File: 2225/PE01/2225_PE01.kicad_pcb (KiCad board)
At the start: 2 copper layers, 95 parts, among them J4 Conn_01x01_Male

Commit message: Added rough board outline to PCB (dimensions are wrong).
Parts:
- moved CE3 45.1 mm to (216.4, 128.4)
- moved RE15 45.1 mm to (227.1, 132.3)
- moved CE12 45.1 mm to (249.7, 170.6)
- moved CE23 45.1 mm to (92.7, 143.0)
- moved CE24 45.1 mm to (92.7, 150.9)
- moved RE43 45.1 mm to (124.5, 133.8)
- moved 100k1 45.1 mm to (300.8, 145.6)
- moved 100k2 45.1 mm to (210.9, 148.1)
- moved CE10 45.1 mm to (270.8, 166.6)
- moved CE13 45.1 mm to (109.7, 159.8)
- moved CE14 45.1 mm to (109.7, 148.4)
- moved CE15 45.1 mm to (142.2, 167.8)
- moved CE17 45.1 mm to (183.9, 150.9)
- moved CE19 45.1 mm to (160.3, 131.0)
- moved CE2 45.1 mm to (332.5, 114.4)
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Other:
- board outline added: 281.9 x 71.4 mm

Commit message: Set PCB component positions to match holes on donor board
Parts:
- CE10, CE9: footprint Capacitor_THT:C_Rect_L7.2mm_W3.5mm_P5.00mm_FKS2_FKP2_MKS2_MKP2 -> Capacitor_THT:C_Rect_L7.2mm_W3.5mm_P8.50mm
- CE19, CE20: footprint Capacitor_THT:CP_Radial_D5.0mm_P2.50mm -> Capacitor_THT:CP_Electrolytic_Radial_D4.5mm_P6.50mm
- CE21: footprint Capacitor_THT:CP_Radial_D6.3mm_P2.50mm -> Capacitor_THT:CP_Radial_D6.3mm_P5.0mm
- CE22, CE3: footprint Capacitor_THT:CP_Radial_D6.3mm_P2.50mm -> Capacitor_THT:CP_Radial_D6.3mm_H11.0mm_P3.50mm
- CE23, CE24: footprint Capacitor_THT:C_Radial_D6.3mm_H11.0mm_P2.50mm -> Capacitor_THT:C_Radial_D6.3mm_H11.0mm_P3.50mm
- CE4: footprint Capacitor_THT:CP_Radial_D6.3mm_P2.50mm -> Capacitor_THT:CP_Radial_D7.0mm_P5.00mm
- CE5, CE6: footprint Capacitor_THT:CP_Radial_D5.0mm_P2.50mm -> Capacitor_THT:CP_Electrolytic_Radial_D5.5mm_P8.50mm
- CE7, CE8: footprint Capacitor_THT:C_Disc_D7.0mm_W2.5mm_P5.00mm -> Capacitor_THT:C_Disc_D7.0mm_W2.5mm_P6.00mm
- HE1, HE2, HE3, HE4, HE5, HE6, HE7, HE8: footprint Package_TO_SOT_THT:TO-92_Inline -> Package_TO_SOT_THT:TO-92_Inline_Wide_10mm
- RE1, RE10, RE12, RE19, RE2, RE20, RE3, RE4, RE40, RE47, RE49, RE50, RE54, RE7, RE8: footprint Resistor_THT:R_Axial_DIN0309_L9.0mm_D3.2mm_P12.70mm_Horizontal -> Resistor_THT:R_Axial_DIN0309_L9.0mm_D3.2mm_P12.50mm_Horizontal
- RE15: footprint Resistor_THT:R_Axial_DIN0309_L9.0mm_D3.2mm_P12.70mm_Horizontal -> Resistor_THT:R_Axial_DIN0309_L9.0mm_D3.2mm_P13.20mm_Horizontal
- RE5, RE6: footprint Resistor_THT:R_Axial_DIN0309_L9.0mm_D3.2mm_P5.08mm_Vertical -> Resistor_THT:R_Axial_DIN0309_L9.0mm_D3.2mm_P5.08mm_Vertical_Flipped
- moved JE1 193.3 mm to (195.0, 41.6)
- moved JE3 191.3 mm to (195.0, 26.0)
- moved JE2 191.1 mm to (195.0, 11.0)
- moved RE1 190.5 mm to (190.0, 30.0)
- moved RE2 189.1 mm to (190.0, 26.0)
- moved CE1 183.0 mm to (187.0, 51.5)
- moved RE24 182.8 mm to (140.0, 37.5)
- moved CE7 182.5 mm to (156.0, 44.0)
- moved RE22 182.4 mm to (150.0, 39.0)
- moved CE2 182.0 mm to (187.0, 5.00)
- moved RE21 181.4 mm to (146.0, 39.0)
- moved CE8 181.2 mm to (152.5, 39.5)
- moved JE5 180.0 mm to (160.0, 6.00)
- moved JE4 179.4 mm to (173.0, 6.00)
- moved RE5 178.7 mm to (164.5, 21.5)
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- renumbered J4 to JE4
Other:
- board size 281.9 x 71.4 mm -> 200 x 60 mm

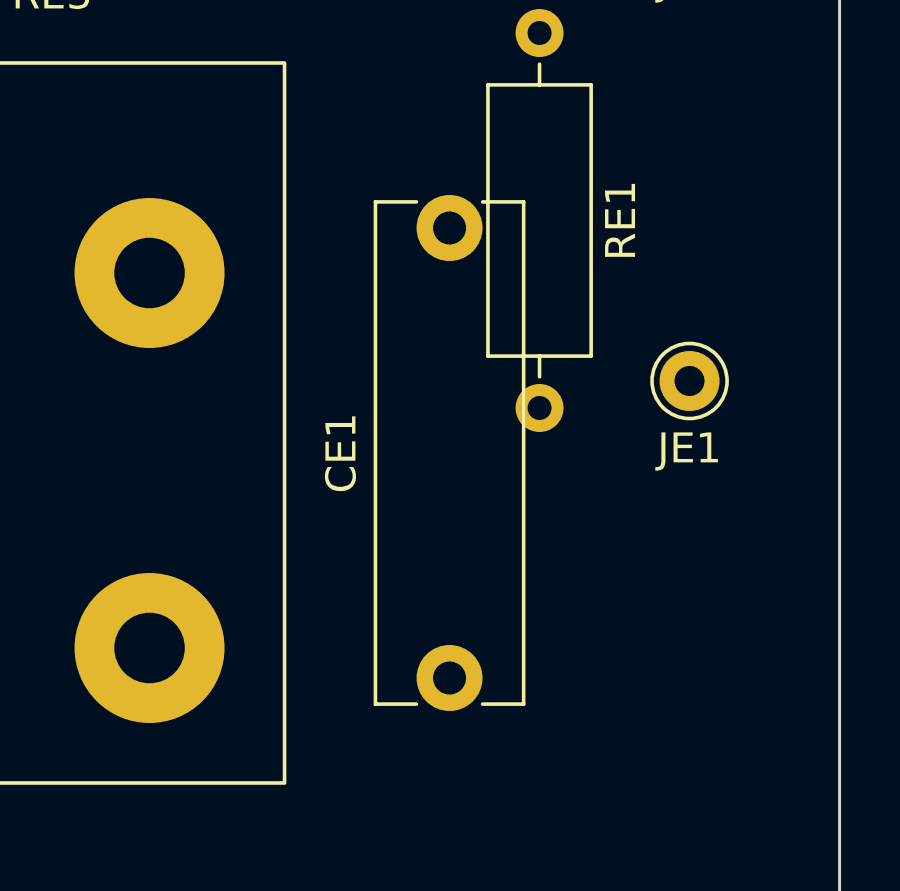
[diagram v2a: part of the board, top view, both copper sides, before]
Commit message: Fixed CE1, which was upside down on pcb layout
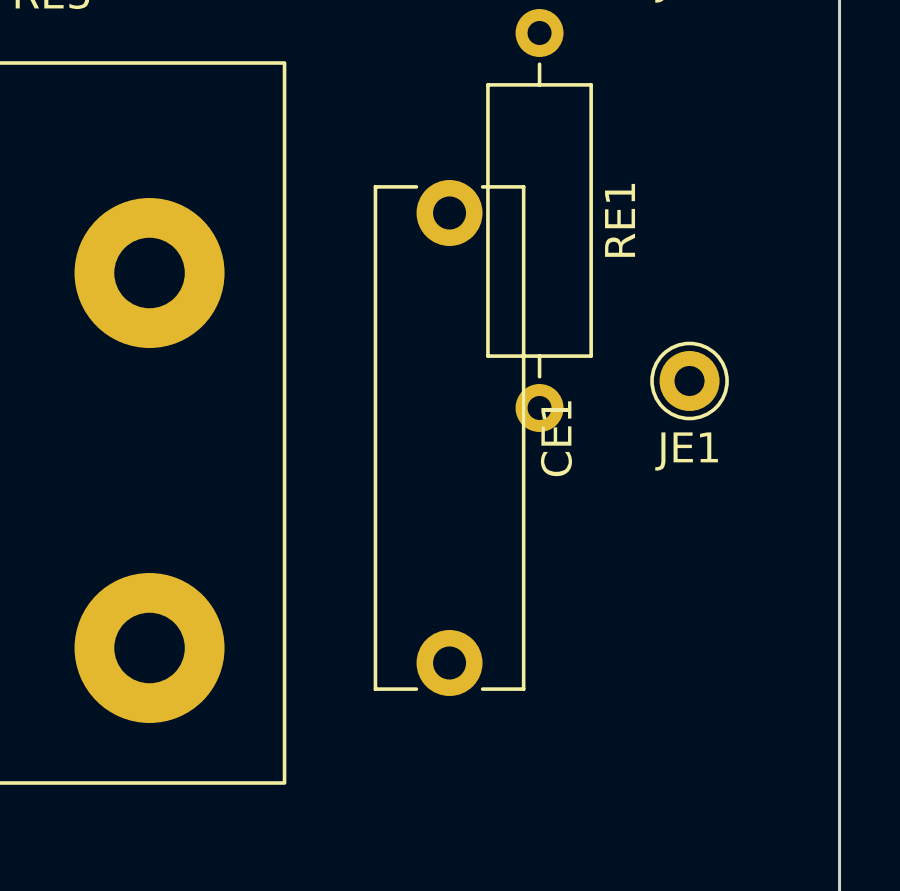
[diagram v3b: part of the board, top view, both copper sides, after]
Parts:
- moved CE1 15.5 mm to (187.0, 36.0), turned to -90 degrees
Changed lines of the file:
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@@
   )
   (setup
+    (stackup
+      (layer "F.SilkS" (type "Top Silk Screen"))
+      (layer "F.Paste" (type "Top Solder Paste"))
+      (layer "F.Mask" (type "Top Solder Mask") (thickness 0.01))
+      (layer "F.Cu" (type "copper") (thickness 0.035))
+      (layer "dielectric 1" (type "core") (thickness 1.51) (material "FR4") (epsilon_r 4.5) (loss_tangent 0.02))
+      (layer "B.Cu" (type "copper") (thickness 0.035))
+      (layer "B.Mask" (type "Bottom Solder Mask") (thickness 0.01))
+      (layer "B.Paste" (type "Bottom Solder Paste"))
+      (layer "B.SilkS" (type "Bottom Silk Screen"))
+      (copper_finish "None")
+      (dielectric_constraints no)
+    )
     (pad_to_mask_clearance 0)
     (pcbplotparams
@@
   )
   (footprint "Capacitor_THT:C_Rect_L16.5mm_W4.7mm_P15.00mm_MKT" (layer "F.Cu")
-    (at 187 51.5 90)
+    (at 187 36 -90)
     (descr "C, Rect series, Radial, pin pitch=15.00mm, , length*width=16.5*4.7mm^2, Capacitor, https://en.tdk.eu/inf/20/20/db/fc_2009/MKT_B32560_564.pdf")
     (tags "C Rect series Radial pin pitch 15.00mm  length 16.5mm width 4.7mm Capacitor")
@@
     (fp_line (start -0.75 -2.35) (end -0.75 2.35) (layer "F.Fab") (width 0.1))
     (fp_line (start 15.75 2.35) (end 15.75 -2.35) (layer "F.Fab") (width 0.1))
-    (pad "1" thru_hole circle (at 0 0 90) (size 2.2 2.2) (drill 1.1) (layers *.Cu *.Mask)
+    (pad "1" thru_hole circle (at 0 0 270) (size 2.2 2.2) (drill 1.1) (layers *.Cu *.Mask)
       (net 19 "Net-(CE1-Pad1)") (pintype "passive"))
-    (pad "2" thru_hole circle (at 15 0 90) (size 2.2 2.2) (drill 1.1) (layers *.Cu *.Mask)
+    (pad "2" thru_hole circle (at 15 0 270) (size 2.2 2.2) (drill 1.1) (layers *.Cu *.Mask)
       (net 20 "Net-(CE1-Pad2)") (pintype "passive"))
     (model "${KICAD6_3DMODEL_DIR}/Capacitor_THT.3dshapes/C_Rect_L16.5mm_W4.7mm_P15.00mm_MKT.wrl"

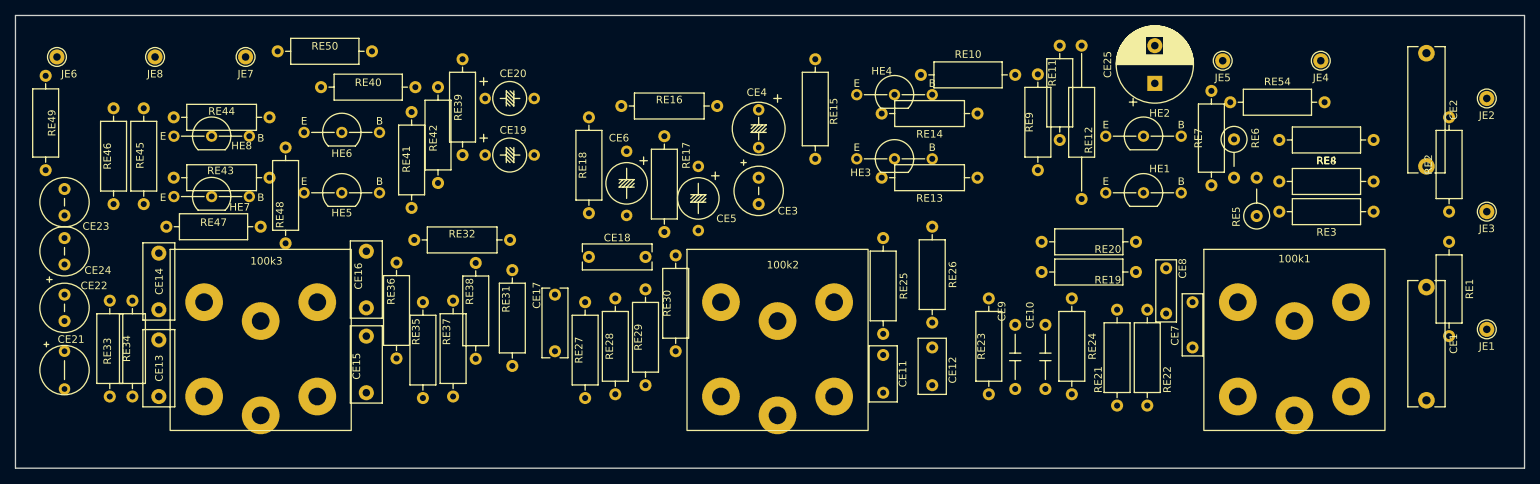
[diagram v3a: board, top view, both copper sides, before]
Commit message: Fixed short circuit across RE8. Added traces. Still need ground plane.
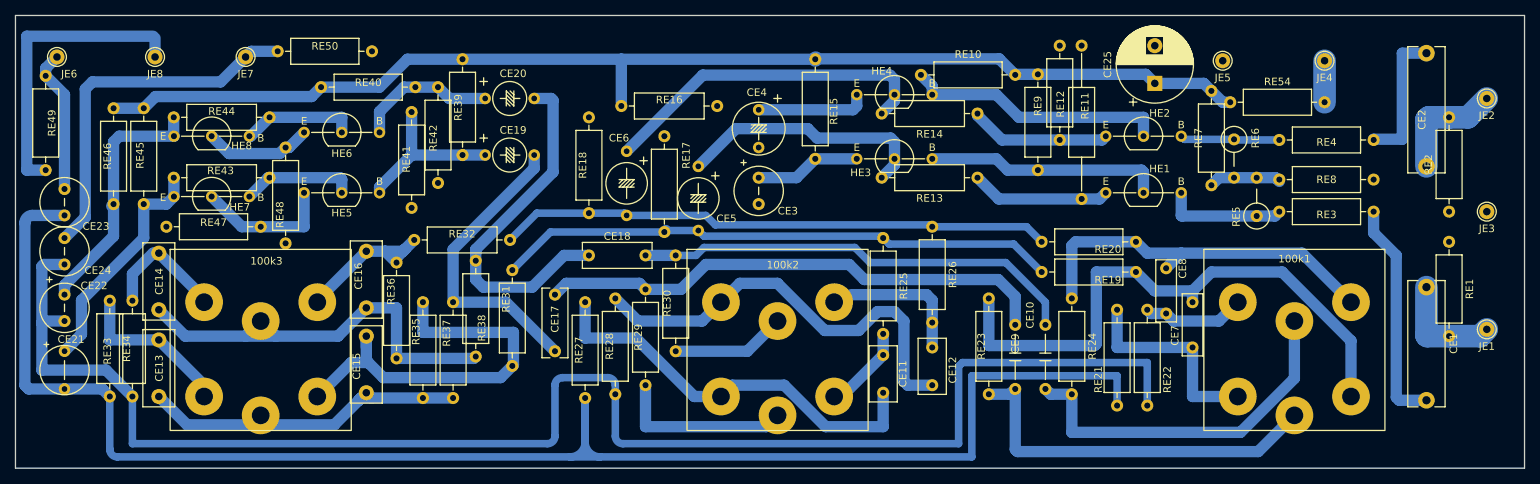
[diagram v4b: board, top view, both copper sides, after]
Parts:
- moved CE2 15.0 mm to (187.0, 20.0), turned to 90 degrees
- moved RE38 13.0 mm to (61.0, 32.5), turned to -90 degrees
- moved RE8 12.5 mm to (180.0, 21.8), turned to 180 degrees
- moved JE4 0.50 mm to (173.5, 6.00)
- moved RE37 0.20 mm to (58.0, 50.7)
- moved CE18 0.20 mm to (83.5, 31.8)
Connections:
- RE5 pad 1: Net-(CE25-Pad2) -> Net-(RE5-Pad1)
- RE6 pad 1: Net-(CE25-Pad2) -> Net-(RE5-Pad1)
- RE7 pad 1: Net-(CE25-Pad2) -> Net-(RE5-Pad1)
- RE8 pad 2: Net-(CE25-Pad2) -> Net-(RE5-Pad1)
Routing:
- net Net-(CE21-Pad2): track 0.00 -> 212.6 mm
- net Net-(CE22-Pad2): track 0.00 -> 205.9 mm
- net Net-(CE25-Pad1): track 0.00 -> 159.3 mm
- net Net-(100k1-Pad3): track 0.00 -> 78.6 mm
- net Net-(CE5-Pad2): track 0.00 -> 74.6 mm
- net Net-(CE6-Pad2): track 0.00 -> 73.5 mm
- net Net-(CE17-Pad1): track 0.00 -> 68.8 mm
- net Net-(CE10-Pad2): track 0.00 -> 59.4 mm
- net Net-(100k2-Pad6): track 0.00 -> 57.7 mm
- net Net-(100k3-Pad5): track 0.00 -> 57.5 mm
- net Net-(100k2-Pad1): track 0.00 -> 54.9 mm
- net Net-(100k3-Pad3): track 0.00 -> 54.8 mm
- net Net-(100k1-Pad2): track 0.00 -> 51.0 mm
- net Net-(100k1-Pad4): track 0.00 -> 50.3 mm
- net Net-(100k1-Pad5): track 0.00 -> 48.9 mm
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
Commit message: Added ground plane.
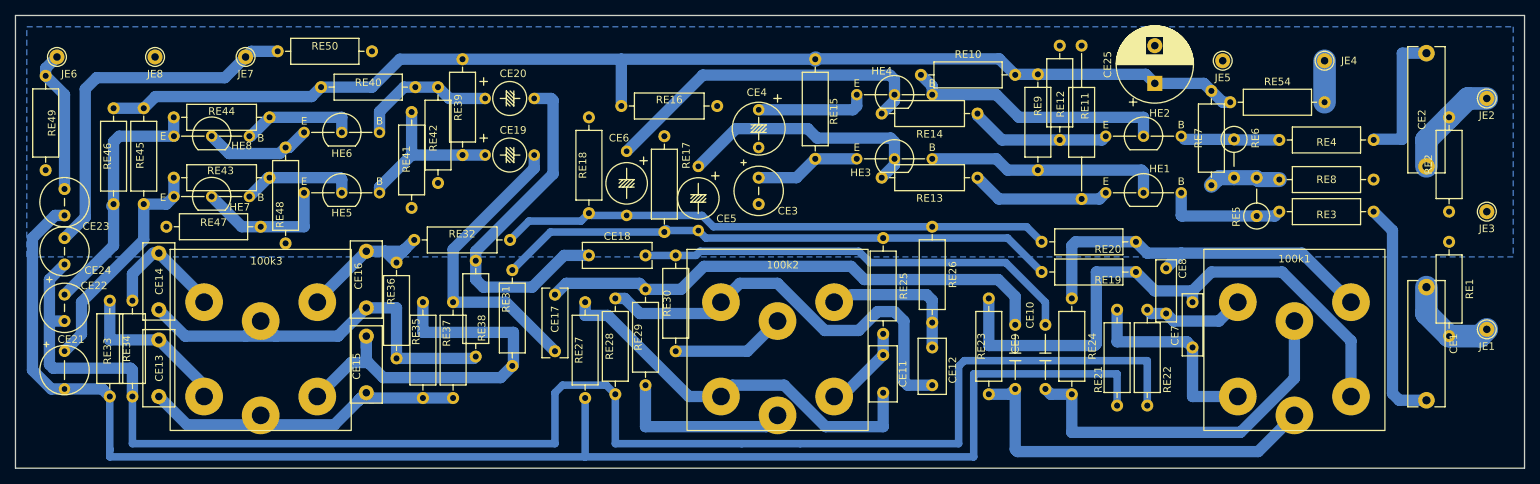
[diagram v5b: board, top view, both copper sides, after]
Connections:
- net Net-(CE25-Pad1) renamed power
- net Net-(CE25-Pad2) renamed ground
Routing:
- net ground: track 39.5 -> 0.00 mm
- net Net-(CE21-Pad2): track 212.6 -> 199.3 mm
- net Net-(CE22-Pad2): track 205.9 -> 202.4 mm
- net Net-(100k2-Pad1): track 54.9 -> 53.1 mm
- net Net-(CE2-Pad1): track 15.4 -> 13.8 mm
- net Net-(CE1-Pad1): track 14.8 -> 13.4 mm
- net Net-(100k2-Pad6): track 57.7 -> 56.8 mm
- added copper zone on B.Cu, net ground

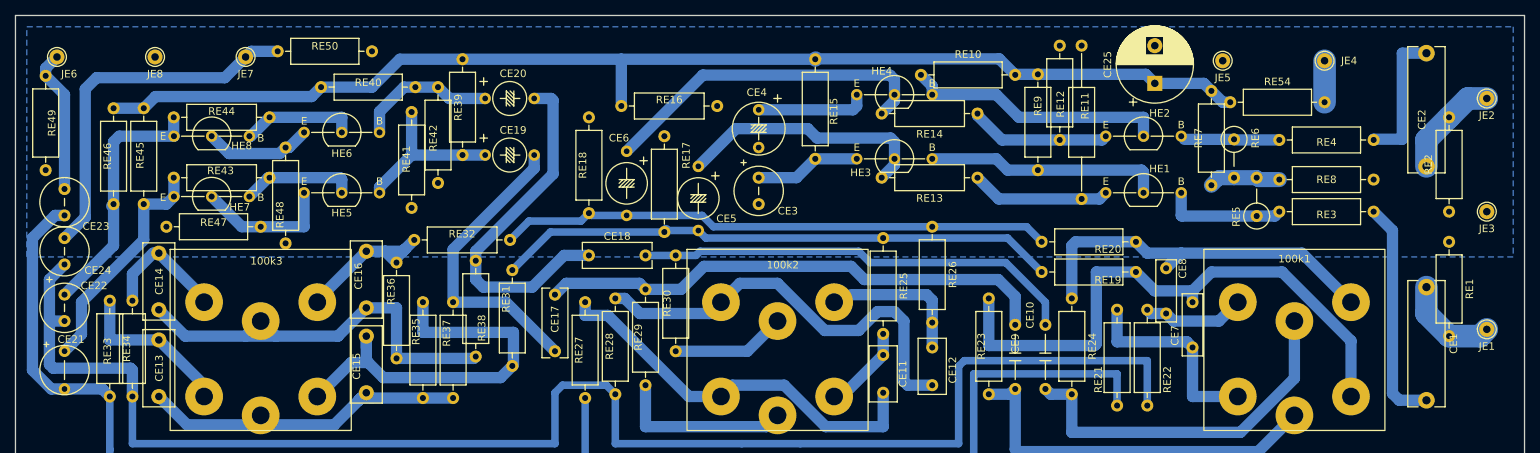
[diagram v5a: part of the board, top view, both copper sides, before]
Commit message: Updated footprint symbols types to match real board (squiggly resistors, etc). Also updated annotations for RE51, RE52, RE53
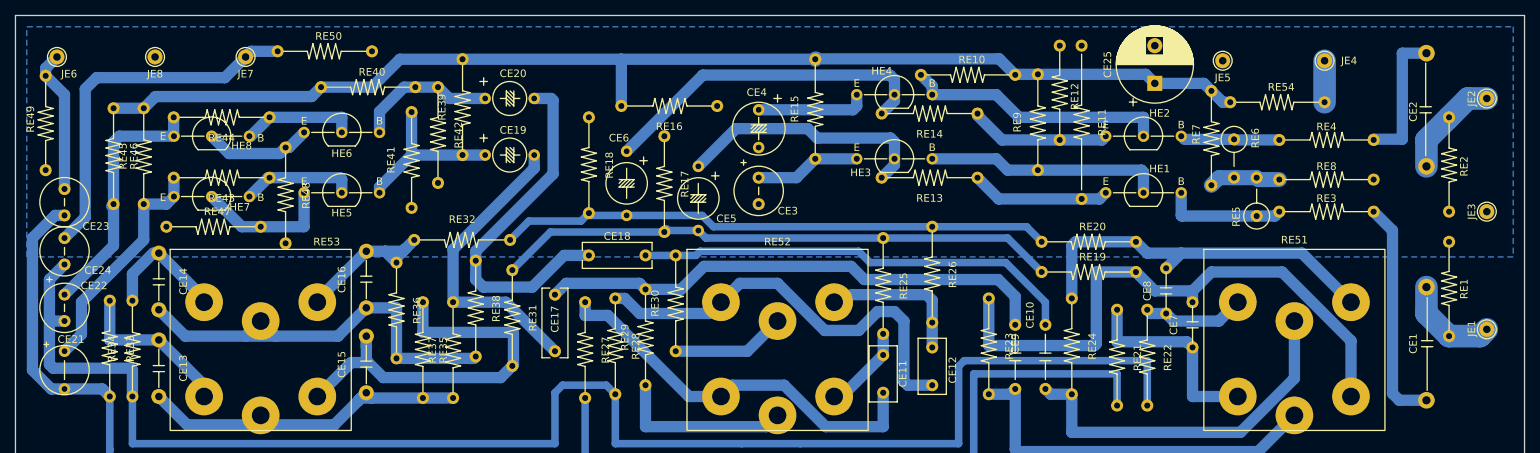
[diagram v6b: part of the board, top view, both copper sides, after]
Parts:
- removed 100k1: RE51(HIGH), Potentiometer_THT:Potentiometer_Marantz_RM0104005
- removed 100k2: RE52(MID), Potentiometer_THT:Potentiometer_Marantz_RM0104005
- removed 100k3: RE53(LOW), Potentiometer_THT:Potentiometer_Marantz_RM0104005
- added RE51: 100k, Potentiometer_THT:Potentiometer_Marantz_RM0104005, F.Cu at (162.0, 50.5)
- added RE52: 100k, Potentiometer_THT:Potentiometer_Marantz_RM0104005, F.Cu at (93.5, 50.5)
- added RE53: 100k, Potentiometer_THT:Potentiometer_Marantz_RM0104005, F.Cu at (25.0, 50.5)
- CE1, CE2: footprint Capacitor_THT:C_Rect_L16.5mm_W4.7mm_P15.00mm_MKT -> Capacitor_THT:C_US_Rect_L16.5mm_W4.7mm_P15.00mm_MKT
- CE13, CE14, CE15, CE16: footprint Capacitor_THT:C_Rect_L10.0mm_W4.0mm_P7.50mm_FKS3_FKP3 -> Capacitor_THT:C_US_Rect_L10.0mm_W4.0mm_P7.50mm_FKS3_FKP3
- CE7, CE8: footprint Capacitor_THT:C_Disc_D7.0mm_W2.5mm_P6.00mm -> Capacitor_THT:C_US_Disc_D7.0mm_W2.5mm_P6.00mm
- RE1, RE10, RE12, RE19, RE2, RE20, RE3, RE4, RE40, RE47, RE49, RE50, RE54, RE7, RE8: footprint Resistor_THT:R_Axial_DIN0309_L9.0mm_D3.2mm_P12.50mm_Horizontal -> Resistor_THT:R_US_Axial_DIN0309_L9.0mm_D3.2mm_P12.50mm_Horizontal
- RE11: footprint Resistor_THT:R_Axial_DIN0309_L9.0mm_D3.2mm_P20.32mm_Horizontal -> Resistor_THT:R_US_Axial_DIN0309_L9.0mm_D3.2mm_P20.32mm_Horizontal
- RE13, RE14, RE16, RE17, RE18, RE21, RE22, RE23, RE24, RE25, RE26, RE27, RE28, RE29, RE30, RE31, RE32, RE33, RE34, RE35, RE36, RE37, RE38, RE39, RE41, RE42, RE43, RE44, RE45, RE46, RE48, RE9: footprint Resistor_THT:R_Axial_DIN0309_L9.0mm_D3.2mm_P12.70mm_Horizontal -> Resistor_THT:R_US_Axial_DIN0309_L9.0mm_D3.2mm_P12.70mm_Horizontal
- RE15: footprint Resistor_THT:R_Axial_DIN0309_L9.0mm_D3.2mm_P13.20mm_Horizontal -> Resistor_THT:R_US_Axial_DIN0309_L9.0mm_D3.2mm_P13.20mm_Horizontal
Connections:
- net ground renamed Net-(CE25-Pad2)
- net power renamed Net-(CE25-Pad1)
